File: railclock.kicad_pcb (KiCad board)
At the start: 2 copper layers, 99.6 x 99.9 mm, 177 parts, among them J1 Conn_01x02_Pin, J10 Conn_01x04_MountingPin, J11 Conn_01x04_MountingPin, J12 Conn_01x04_MountingPin, J13 Conn_01x04_MountingPin, J14 Conn_01x04_MountingPin, J15 Conn_01x03_MountingPin, J16 Barrel_Jack_Switch, J2 Conn_01x03_MountingPin, J3 Conn_01x04_MountingPin, J4 USB_C_Receptacle_USB2.0_14P, J5 Conn_01x03_MountingPin, J6 Conn_01x03_MountingPin, J7 Conn_01x03_MountingPin, J8 Conn_01x03_MountingPin, J9 Conn_01x04_MountingPin, Q1 Q_NPN_BEC, SW1 SW_SPST, SW2 SW_DPDT_x2, U1 MCP7940N-xST, U10 74AHC1G04, U11 MAX811TEUS-T, U12 MCP4728, U13 BTS5012SDA, U14 BTS5012SDA, U15 BTS5012SDA, U16 BTS5012SDA, U17 BTS5012SDA, U2 MCP73832-2-OT, U4 ESP32-C6-WROOM-1, U5 DRV8870DDA, U6 PAM2421, U8 BQ24296MRGET, U9 PCF8574RGTR, Y2 Crystal_GND3

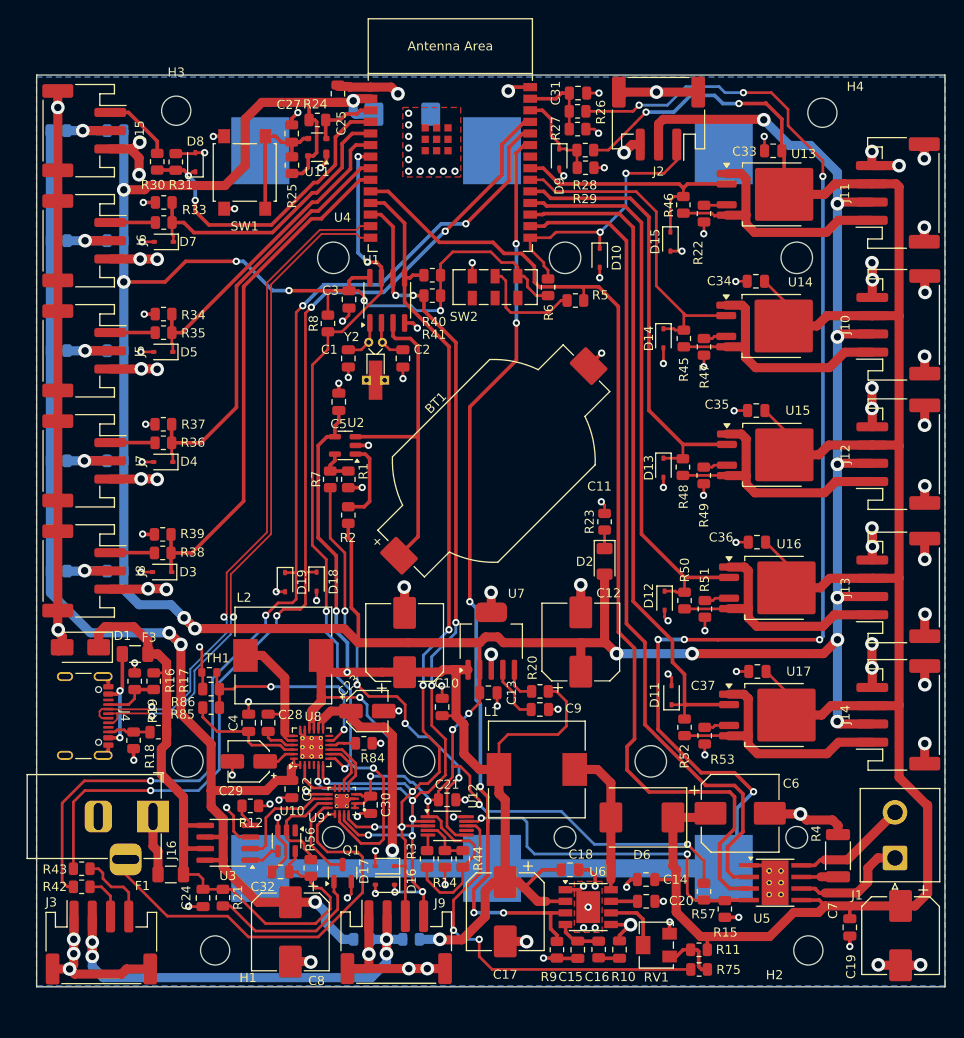
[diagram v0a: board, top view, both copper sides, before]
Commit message: Reroute to 4 layer pcb
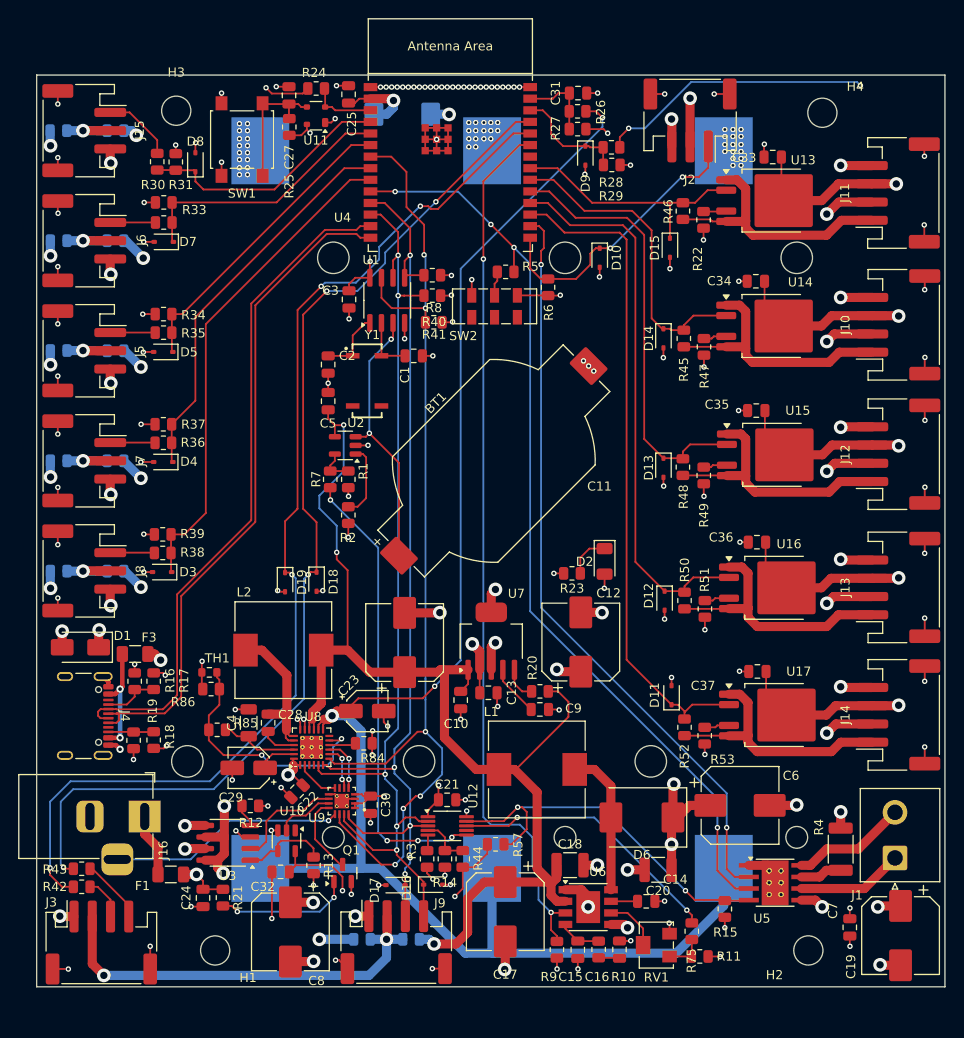
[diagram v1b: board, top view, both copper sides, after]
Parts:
- removed R56: 100k, Resistor_SMD:R_0805_2012Metric
- removed Y2: Crystal_GND3, Crystal:Crystal_DS10_D1.0mm_L4.3mm_Horizontal_1EP_style2
- added R13: 10K, Resistor_SMD:R_0805_2012Metric, F.Cu at (75.1, 110.3)
- added Y1: MC-306_32.7680K-A5__ROHS, th:OSCL550P800X320X254-4N, F.Cu at (80.9, 57.1)
- C17, C19: value C_Polarized -> 470uF 25V
- C18, C20: value C -> 10uF 50V; footprint Capacitor_SMD:C_0805_2012Metric -> Capacitor_SMD:C_1210_3225Metric
- C23: value C_Polarized -> 22uF 16V
- C28: value C -> 47nF
- C29: value C_Polarized -> 8.2uF
- C4: value C -> 4.7uF; footprint Capacitor_SMD:C_0805_2012Metric -> Capacitor_SMD:C_1206_3216Metric
- D6: value D -> SS34
- L1: value L -> 6.8uH
- moved R57 23.4 mm to (95.0, 108.0), turned to 0 degrees
- moved R8 11.6 mm to (88.2, 50.7), turned to 180 degrees
- moved R5 8.27 mm to (96.1, 45.2)
- moved C2 8.22 mm to (76.7, 55.4)
- moved C1 7.17 mm to (86.0, 54.4), turned to 0 degrees
- moved R23 6.69 mm to (103.4, 78.2), turned to 180 degrees
- moved D16 5.28 mm to (88.2, 112.4), turned to 0 degrees
- moved R75 4.27 mm to (116.5, 117.5), turned to 90 degrees
- moved C27 4.19 mm to (72.4, 25.8)
- moved R25 4.19 mm to (72.4, 29.3)
- moved SW1 3.62 mm to (67.2, 30.7)
- moved J2 3.47 mm to (116.3, 28.6)
- moved R24 3.46 mm to (75.3, 25.1)
- moved U11 3.46 mm to (75.3, 28.1)
- moved D9 2.89 mm to (104.9, 32.5)
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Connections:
- C1 pad 1: Net-(U1-X1) -> Net-(U1-X2)
- C2 pad 1: Net-(U1-X2) -> Net-(U1-X1)
- C32 pad 1: VBUS -> +3.3V
- U10 pad 5: VBUS -> +3.3V
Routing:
- net +3.3V: track 465.8 -> 116.3 mm, vias 24 -> 28
- net +12V: track 253.4 -> 144.7 mm, vias 2 -> 13
- net +5V: track 130.1 -> 31.2 mm, vias 3 -> 10
- net GND: track 349.8 -> 263.1 mm, vias 141 -> 212
- net VBUS: track 73.7 -> 16.5 mm, vias 0 -> 7
- net +BATT: track 212.8 -> 178.0 mm, vias 8 -> 3
- net DC_JACK_PRESENT: track 46.3 -> 25.0 mm, vias 0 -> 1
- net GLOBAL_INT: track 96.2 -> 114.8 mm, vias 5 -> 6
- net DAC_CH3: track 42.7 -> 30.4 mm
- net BOOT0: track 113.1 -> 102.8 mm, vias 0 -> 4
- net Net-(SW2A-B): track 11.8 -> 2.70 mm
- net SCL: track 115.3 -> 106.6 mm, vias 11 -> 5
- net MOTOR_IN2: track 91.1 -> 83.0 mm, vias 0 -> 2
- net ADC2: track 35.2 -> 28.0 mm, vias 2 -> 0
- net VPP: track 138.9 -> 131.8 mm, vias 4 -> 3
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- added copper zone on In2.Cu, net +12V
- added copper zone on In2.Cu, net +3.3V
- added copper zone on In2.Cu, net +5V
- added copper zone on In1.Cu, net GND
- added copper zone on In2.Cu, net VBUS
- removed copper zone on B.Cu, net GND
- removed copper zone on F.Cu, net GND
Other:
- copper layers 2 -> 4

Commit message: Rework to new kanapka
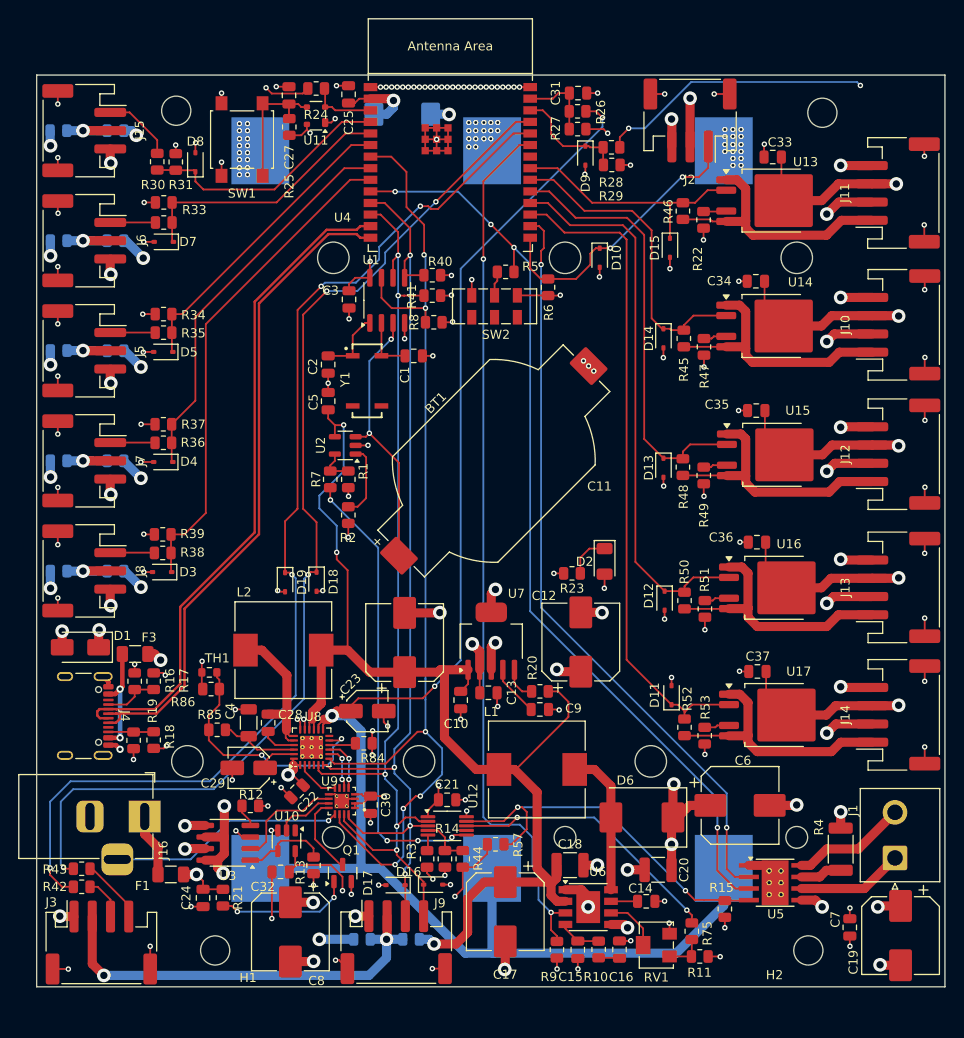
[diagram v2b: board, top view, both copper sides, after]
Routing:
- net USB+: track 73.1 -> 72.5 mm
- net SDA: vias 5 -> 4
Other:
- board text added: "5V IN"
- board text added: "A0"
- board text added: "A1"
- board text added: "A2"
- board text added: "A3"
- board text added: "A4"
- board text added: "D0"
- board text added: "D1"
- board text added: "D2"
- board text added: "D3"
- board text added: "D4"
- board text added: "I2C"
- board text added: "Motor"
- board text added: "UART"
- board text added: "USB-C"

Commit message: Fix VBUS detection and add wakeup button
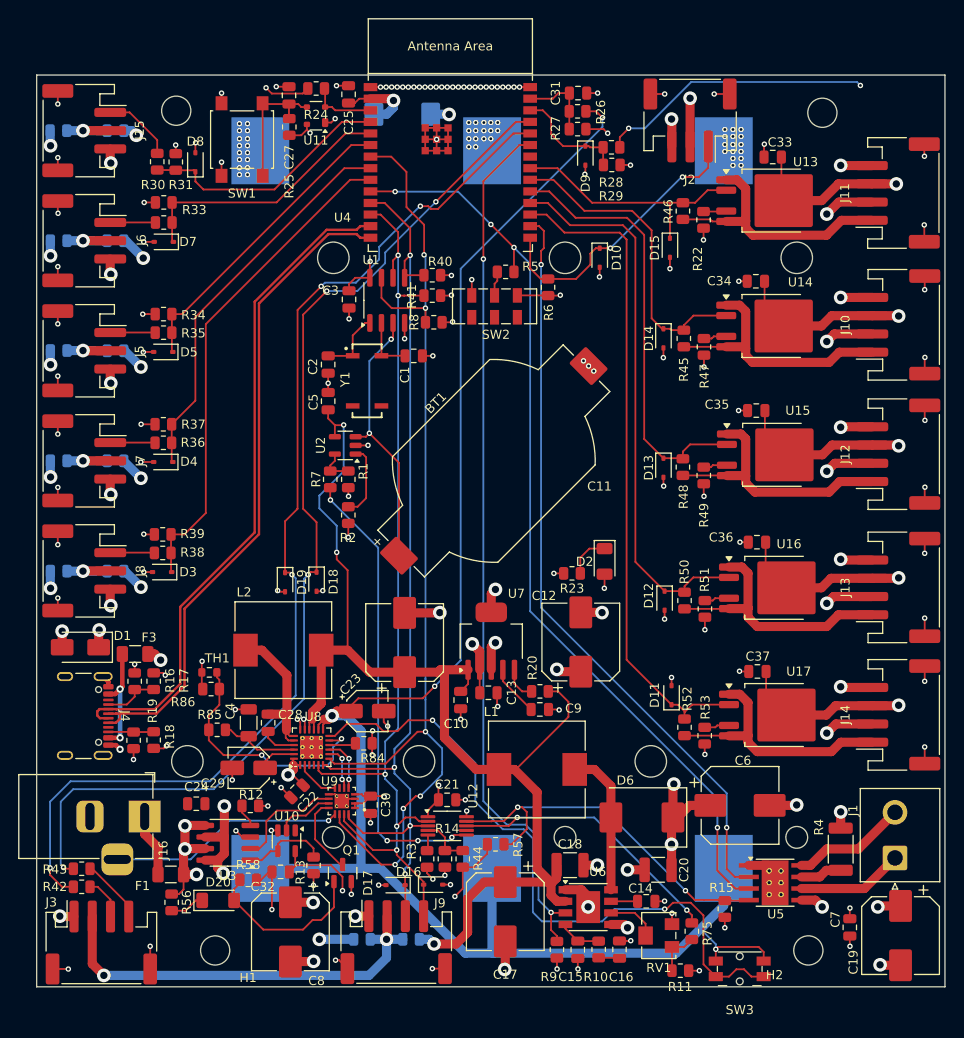
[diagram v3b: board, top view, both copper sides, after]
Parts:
- removed R21: R, Resistor_SMD:R_0805_2012Metric
- added D20: BZV55B7V5, Diode_SMD:D_MiniMELF, F.Cu at (64.6, 114.1)
- added R56: R, Resistor_SMD:R_0805_2012Metric, F.Cu at (59.5, 114.3)
- added R58: R, Resistor_SMD:R_0805_2012Metric, F.Cu at (67.9, 111.8)
- added SW3: SW_SPST, Button_Switch_SMD:Panasonic_EVQPUL_EVQPUC, F.Cu at (121.8, 121.6)
- moved C24 10.4 mm to (62.2, 103.5), turned to 180 degrees
- moved R11 2.64 mm to (115.3, 121.8)
- moved RV1 1.08 mm to (112.9, 118.0)
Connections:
- U8 pad 12: unconnected-(U8-QON-Pad12) -> WAKEUP
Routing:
- net WAKEUP: track 0.00 -> 73.4 mm, vias 0 -> 2
- net +BATT: track 178.0 -> 188.8 mm, vias 3 -> 4
- net VBUS: track 16.5 -> 21.0 mm
- net Net-(D20-K): track 0.00 -> 3.82 mm
- net Net-(D20-A): track 14.8 -> 18.6 mm, vias 2 -> 0
- net Net-(R11-Pad2): track 4.27 -> 5.11 mm
- net BOOST_EN: track 96.9 -> 96.2 mm
- net GND: track 263.1 -> 262.8 mm, vias 212 -> 211
